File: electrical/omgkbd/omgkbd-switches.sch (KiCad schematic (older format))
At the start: 61 parts

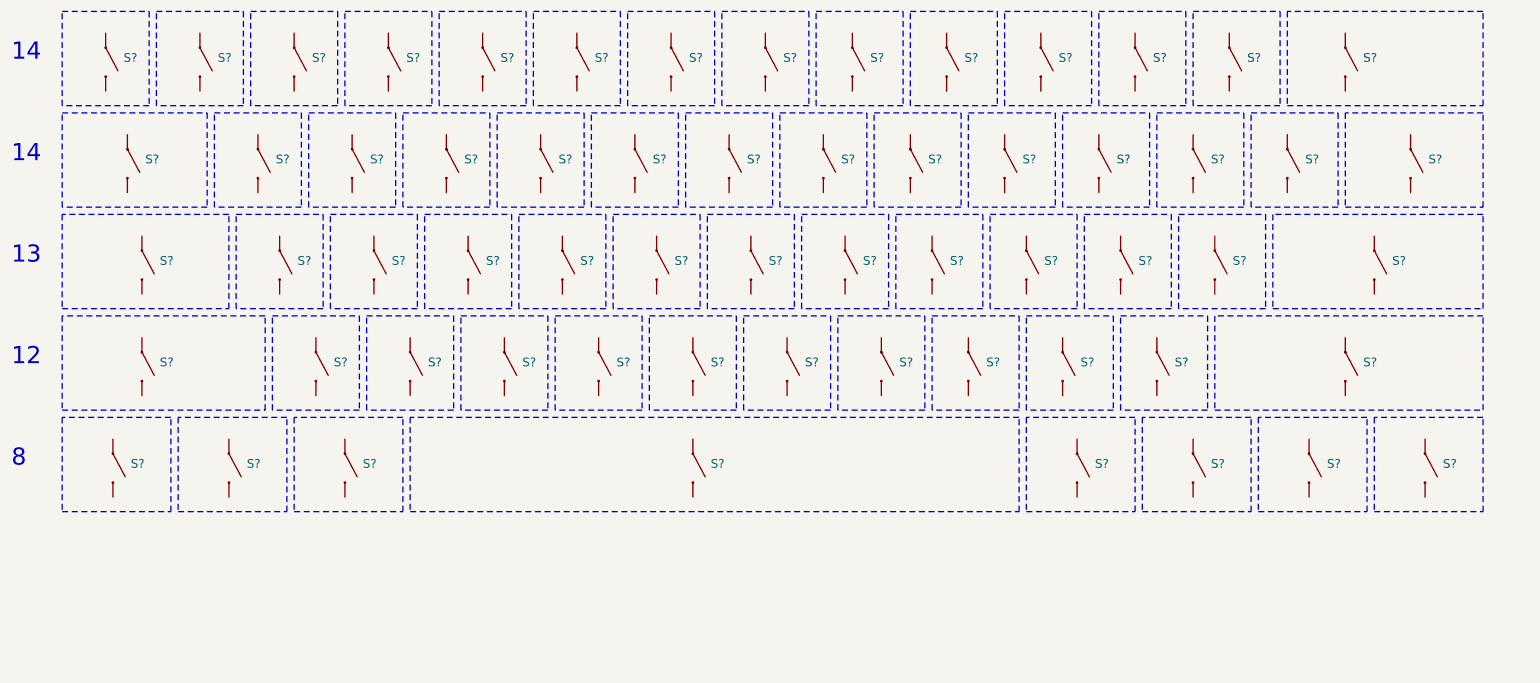
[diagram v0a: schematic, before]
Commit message: Added switches, back and ambient light schematics
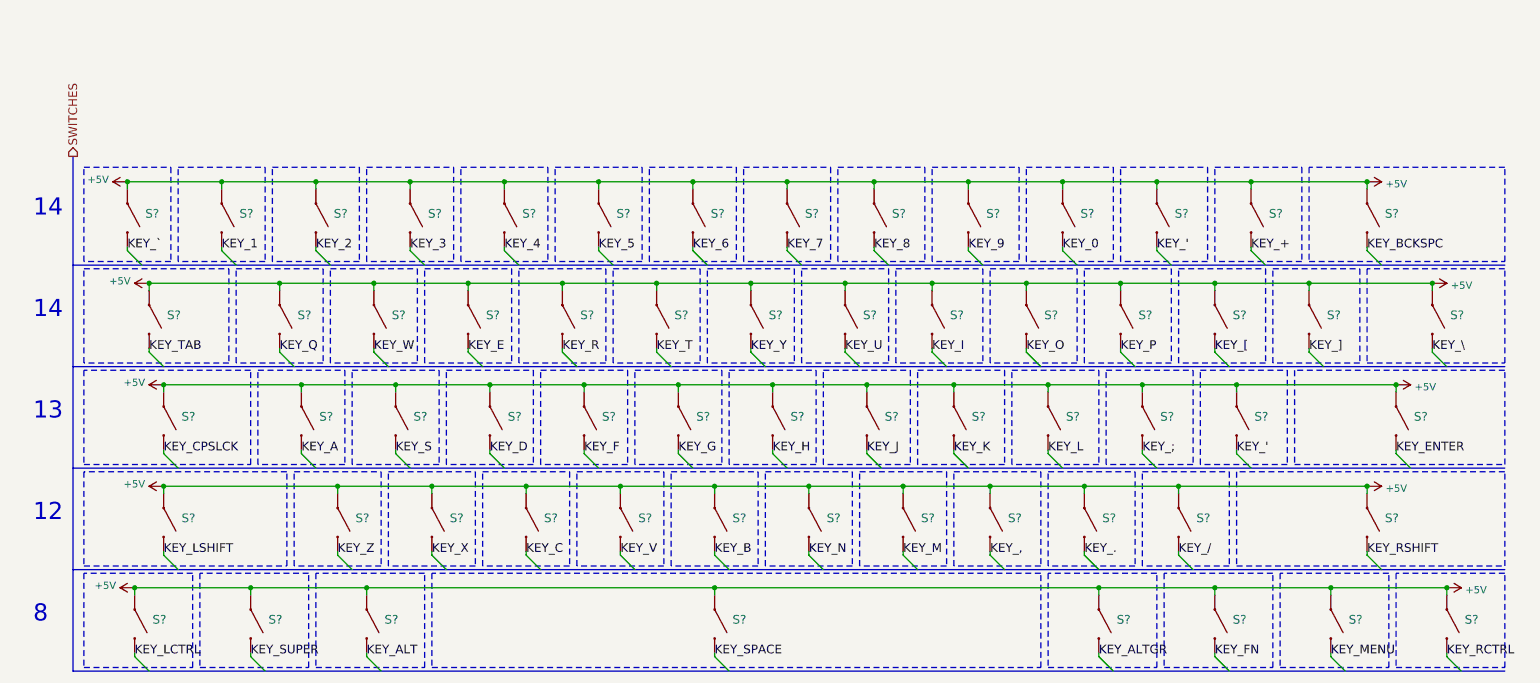
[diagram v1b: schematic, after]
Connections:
- net +5V: now reaches S?.1
- net +5V: now also S?.1, S?.1, S?.1, S?.1, S?.1, S?.1, S?.1, S?.1, S?.1, S?.1, S?.1, S?.1, S?.1, S?.1, S?.1, S?.1, S?.1, S?.1, S?.1, S?.1, S?.1, S?.1, S?.1, S?.1, S?.1, S?.1, S?.1, S?.1, S?.1, S?.1, S?.1, S?.1, S?.1, S?.1, S?.1, S?.1, S?.1, S?.1, S?.1, S?.1, S?.1, S?.1, S?.1, S?.1, S?.1, S?.1, S?.1, S?.1, S?.1, S?.1, S?.1, S?.1, S?.1, S?.1, S?.1, S?.1, S?.1, S?.1, S?.1, S?.1
- net KEY_`: now reaches S?.2
- net KEY_1: now reaches S?.2
- net KEY_2: now reaches S?.2
- net KEY_3: now reaches S?.2
- net KEY_4: now reaches S?.2
- net KEY_5: now reaches S?.2
- net KEY_6: now reaches S?.2
- net KEY_7: now reaches S?.2
- net KEY_8: now reaches S?.2
- net KEY_9: now reaches S?.2
- net KEY_0: now reaches S?.2
- net KEY_': now reaches S?.2
- net KEY_': now also S?.2
- net KEY_+: now reaches S?.2
- net KEY_BCKSPC: now reaches S?.2
- net KEY_TAB: now reaches S?.2
- net KEY_Q: now reaches S?.2
- net KEY_W: now reaches S?.2
- net KEY_E: now reaches S?.2
- net KEY_R: now reaches S?.2
- net KEY_T: now reaches S?.2
- net KEY_Y: now reaches S?.2
- net KEY_U: now reaches S?.2
- net KEY_I: now reaches S?.2
- net KEY_O: now reaches S?.2
- net KEY_P: now reaches S?.2
- net KEY_[: now reaches S?.2
- net KEY_]: now reaches S?.2
- net KEY_\: now reaches S?.2
- net KEY_CPSLCK: now reaches S?.2
- net KEY_A: now reaches S?.2
- net KEY_S: now reaches S?.2
- net KEY_D: now reaches S?.2
- net KEY_F: now reaches S?.2
- net KEY_G: now reaches S?.2
- net KEY_H: now reaches S?.2
- net KEY_J: now reaches S?.2
- net KEY_K: now reaches S?.2
- net KEY_L: now reaches S?.2
- net KEY_;: now reaches S?.2
- net KEY_ENTER: now reaches S?.2
- net KEY_LSHIFT: now reaches S?.2
- net KEY_Z: now reaches S?.2
- net KEY_X: now reaches S?.2
- net KEY_C: now reaches S?.2
- net KEY_V: now reaches S?.2
- net KEY_B: now reaches S?.2
- net KEY_N: now reaches S?.2
- net KEY_M: now reaches S?.2
- net KEY_,: now reaches S?.2
- net KEY_.: now reaches S?.2
- net KEY_/: now reaches S?.2
- net KEY_RSHIFT: now reaches S?.2
- net KEY_LCTRL: now reaches S?.2
- net KEY_SUPER: now reaches S?.2
- net KEY_ALT: now reaches S?.2
- net KEY_RCTRL: now reaches S?.2
- net KEY_MENU: now reaches S?.2
- net KEY_FN: now reaches S?.2
- net KEY_ALTGR: now reaches S?.2
- net KEY_SPACE: now reaches S?.2
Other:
- moved on the sheet: S?

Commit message: Started working on connector and power
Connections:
- net +5V renamed +3V3
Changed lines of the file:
@@
 $Descr A4 11693 8268
 encoding utf-8
-Sheet 3 5
+Sheet 3 6
 Title "omgkbd__"
 Date "2017-10-31"
@@
 Connection ~ 2500 3025
 Wire Wire Line
-	1600 3025 1600 3075
-Wire Wire Line
 	2100 2375 2100 2325
 Connection ~ 2100 2325
 Wire Wire Line
 	1450 2375 1450 2325
-$Comp
-L +5V #PWR?
-U 1 1 5A022C9B
-P 1500 5125
-F 0 "#PWR?" H 1500 4975 50  0001 C CNN
-F 1 "+5V" V 1515 5253 50  0000 L CNN
-F 2 "" H 1500 5125 50  0001 C CNN
-F 3 "" H 1500 5125 50  0001 C CNN
-	1    1500 5125
-	0    -1   -1   0
-$EndComp
-$Comp
-L +5V #PWR?
-U 1 1 5A022FD9
-P 1700 4425
-F 0 "#PWR?" H 1700 4275 50  0001 C CNN
-F 1 "+5V" V 1715 4553 50  0000 L CNN
-F 2 "" H 1700 4425 50  0001 C CNN
-F 3 "" H 1700 4425 50  0001 C CNN
-	1    1700 4425
-	0    -1   -1   0
-$EndComp
-$Comp
-L +5V #PWR?
-U 1 1 5A023241
-P 1700 3725
-F 0 "#PWR?" H 1700 3575 50  0001 C CNN
-F 1 "+5V" V 1715 3853 50  0000 L CNN
-F 2 "" H 1700 3725 50  0001 C CNN
-F 3 "" H 1700 3725 50  0001 C CNN
-	1    1700 3725
-	0    -1   -1   0
-$EndComp
-$Comp
-L +5V #PWR?
-U 1 1 5A0234E6
-P 1600 3025
-F 0 "#PWR?" H 1600 2875 50  0001 C CNN
-F 1 "+5V" V 1615 3153 50  0000 L CNN
-F 2 "" H 1600 3025 50  0001 C CNN
-F 3 "" H 1600 3025 50  0001 C CNN
-	1    1600 3025
-	0    -1   -1   0
-$EndComp
-$Comp
-L +5V #PWR?
-U 1 1 5A023711
-P 1450 2325
-F 0 "#PWR?" H 1450 2175 50  0001 C CNN
-F 1 "+5V" V 1465 2453 50  0000 L CNN
-F 2 "" H 1450 2325 50  0001 C CNN
-F 3 "" H 1450 2325 50  0001 C CNN
-	1    1450 2325
-	0    -1   -1   0
-$EndComp
-Connection ~ 1450 2325
-Connection ~ 1600 3025
-Connection ~ 1700 3725
-Connection ~ 1700 4425
-Connection ~ 1500 5125
-$Comp
-L +5V #PWR?
-U 1 1 5A024254
-P 10000 2325
-F 0 "#PWR?" H 10000 2175 50  0001 C CNN
-F 1 "+5V" V 10015 2453 50  0000 L CNN
-F 2 "" H 10000 2325 50  0001 C CNN
-F 3 "" H 10000 2325 50  0001 C CNN
-	1    10000 2325
-	0    1    1    0
-$EndComp
-Connection ~ 10000 2325
-$Comp
-L +5V #PWR?
-U 1 1 5A0248A7
-P 10450 3025
-F 0 "#PWR?" H 10450 2875 50  0001 C CNN
-F 1 "+5V" V 10465 3153 50  0000 L CNN
-F 2 "" H 10450 3025 50  0001 C CNN
-F 3 "" H 10450 3025 50  0001 C CNN
-	1    10450 3025
-	0    1    1    0
-$EndComp
-$Comp
-L +5V #PWR?
-U 1 1 5A024BC6
-P 10200 3725
-F 0 "#PWR?" H 10200 3575 50  0001 C CNN
-F 1 "+5V" V 10215 3853 50  0000 L CNN
-F 2 "" H 10200 3725 50  0001 C CNN
-F 3 "" H 10200 3725 50  0001 C CNN
-	1    10200 3725
-	0    1    1    0
-$EndComp
-$Comp
-L +5V #PWR?
-U 1 1 5A024EE5
-P 10000 4425
-F 0 "#PWR?" H 10000 4275 50  0001 C CNN
-F 1 "+5V" V 10015 4553 50  0000 L CNN
-F 2 "" H 10000 4425 50  0001 C CNN
-F 3 "" H 10000 4425 50  0001 C CNN
-	1    10000 4425
-	0    1    1    0
-$EndComp
-$Comp
-L +5V #PWR?
-U 1 1 5A024F28
-P 10550 5125
-F 0 "#PWR?" H 10550 4975 50  0001 C CNN
-F 1 "+5V" V 10565 5253 50  0000 L CNN
-F 2 "" H 10550 5125 50  0001 C CNN
-F 3 "" H 10550 5125 50  0001 C CNN
-	1    10550 5125
-	0    1    1    0
-$EndComp
-Connection ~ 10550 5125
-Connection ~ 10000 4425
-Connection ~ 10200 3725
-Connection ~ 10450 3025
 Text Label 1450 2800 0    60   ~ 0
 KEY_`
@@
 Text Label 5500 4900 0    60   ~ 0
 KEY_B
+Wire Wire Line
+	1600 3025 1600 3075
+$Comp
+L +3.3V #PWR?
+U 1 1 5A03A8DD
+P 10550 5125
+F 0 "#PWR?" H 10550 4975 50  0001 C CNN
+F 1 "+3.3V" V 10565 5253 50  0000 L CNN
+F 2 "" H 10550 5125 50  0001 C CNN
+F 3 "" H 10550 5125 50  0001 C CNN
+	1    10550 5125
+	0    1    1    0
+$EndComp
+$Comp
+L +3.3V #PWR?
+U 1 1 5A03AB5C
+P 10000 4425
+F 0 "#PWR?" H 10000 4275 50  0001 C CNN
+F 1 "+3.3V" V 10015 4553 50  0000 L CNN
+F 2 "" H 10000 4425 50  0001 C CNN
+F 3 "" H 10000 4425 50  0001 C CNN
+	1    10000 4425
+	0    1    1    0
+$EndComp
+$Comp
+L +3.3V #PWR?
+U 1 1 5A03AB9F
+P 10200 3725
+F 0 "#PWR?" H 10200 3575 50  0001 C CNN
+F 1 "+3.3V" V 10215 3853 50  0000 L CNN
+F 2 "" H 10200 3725 50  0001 C CNN
+F 3 "" H 10200 3725 50  0001 C CNN
+	1    10200 3725
+	0    1    1    0
+$EndComp
+$Comp
+L +3.3V #PWR?
+U 1 1 5A03AFEF
+P 10450 3025
+F 0 "#PWR?" H 10450 2875 50  0001 C CNN
+F 1 "+3.3V" V 10465 3153 50  0000 L CNN
+F 2 "" H 10450 3025 50  0001 C CNN
+F 3 "" H 10450 3025 50  0001 C CNN
+	1    10450 3025
+	0    1    1    0
+$EndComp
+$Comp
+L +3.3V #PWR?
+U 1 1 5A03B163
+P 10000 2325
+F 0 "#PWR?" H 10000 2175 50  0001 C CNN
+F 1 "+3.3V" V 10015 2453 50  0000 L CNN
+F 2 "" H 10000 2325 50  0001 C CNN
+F 3 "" H 10000 2325 50  0001 C CNN
+	1    10000 2325
+	0    1    1    0
+$EndComp
+$Comp
+L +3.3V #PWR?
+U 1 1 5A03B6A7
+P 1450 2325
+F 0 "#PWR?" H 1450 2175 50  0001 C CNN
+F 1 "+3.3V" V 1465 2453 50  0000 L CNN
+F 2 "" H 1450 2325 50  0001 C CNN
+F 3 "" H 1450 2325 50  0001 C CNN
+	1    1450 2325
+	0    -1   -1   0
+$EndComp
+$Comp
+L +3.3V #PWR?
+U 1 1 5A03B8A9
+P 1600 3025
+F 0 "#PWR?" H 1600 2875 50  0001 C CNN
+F 1 "+3.3V" V 1615 3153 50  0000 L CNN
+F 2 "" H 1600 3025 50  0001 C CNN
+F 3 "" H 1600 3025 50  0001 C CNN
+	1    1600 3025
+	0    -1   -1   0
+$EndComp
+$Comp
+L +3.3V #PWR?
+U 1 1 5A03BA9C
+P 1700 3725
+F 0 "#PWR?" H 1700 3575 50  0001 C CNN
+F 1 "+3.3V" V 1715 3853 50  0000 L CNN
+F 2 "" H 1700 3725 50  0001 C CNN
+F 3 "" H 1700 3725 50  0001 C CNN
+	1    1700 3725
+	0    -1   -1   0
+$EndComp
+$Comp
+L +3.3V #PWR?
+U 1 1 5A03BB21
+P 1700 4425
+F 0 "#PWR?" H 1700 4275 50  0001 C CNN
+F 1 "+3.3V" V 1715 4553 50  0000 L CNN
+F 2 "" H 1700 4425 50  0001 C CNN
+F 3 "" H 1700 4425 50  0001 C CNN
+	1    1700 4425
+	0    -1   -1   0
+$EndComp
+$Comp
+L +3.3V #PWR?
+U 1 1 5A03BC9A
+P 1500 5125
+F 0 "#PWR?" H 1500 4975 50  0001 C CNN
+F 1 "+3.3V" V 1515 5253 50  0000 L CNN
+F 2 "" H 1500 5125 50  0001 C CNN
+F 3 "" H 1500 5125 50  0001 C CNN
+	1    1500 5125
+	0    -1   -1   0
+$EndComp
 $EndSCHEMATC
